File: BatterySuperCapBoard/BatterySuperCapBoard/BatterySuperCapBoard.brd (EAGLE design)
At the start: 94 x 88 mm, 18 parts, among them X1 ESQ-126-38-G-D, X2 WEIDMULLER

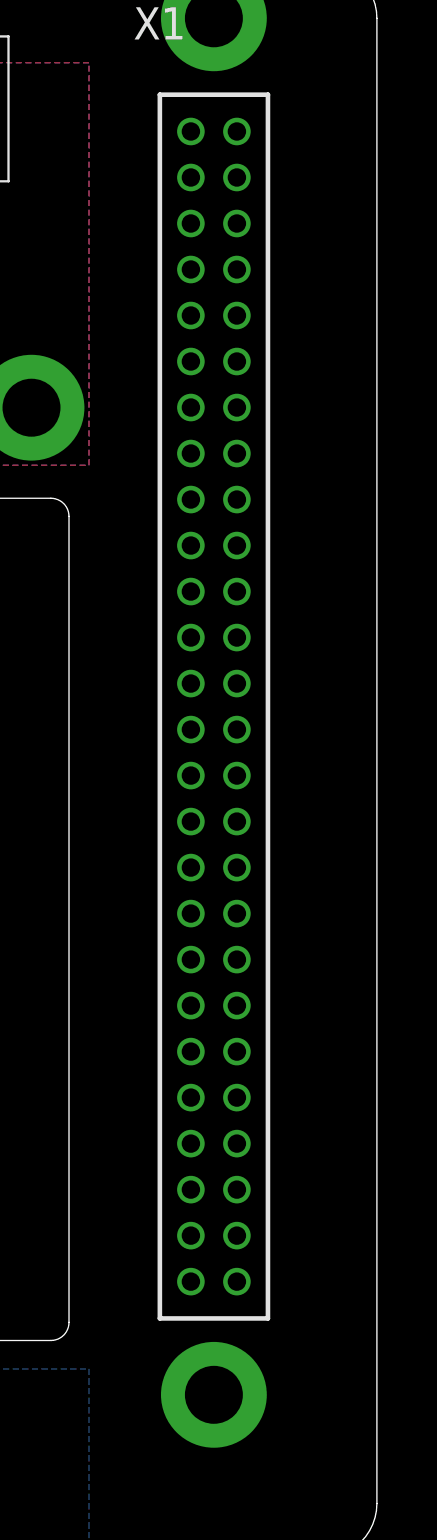
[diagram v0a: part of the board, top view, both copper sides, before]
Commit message: supercap battery board added
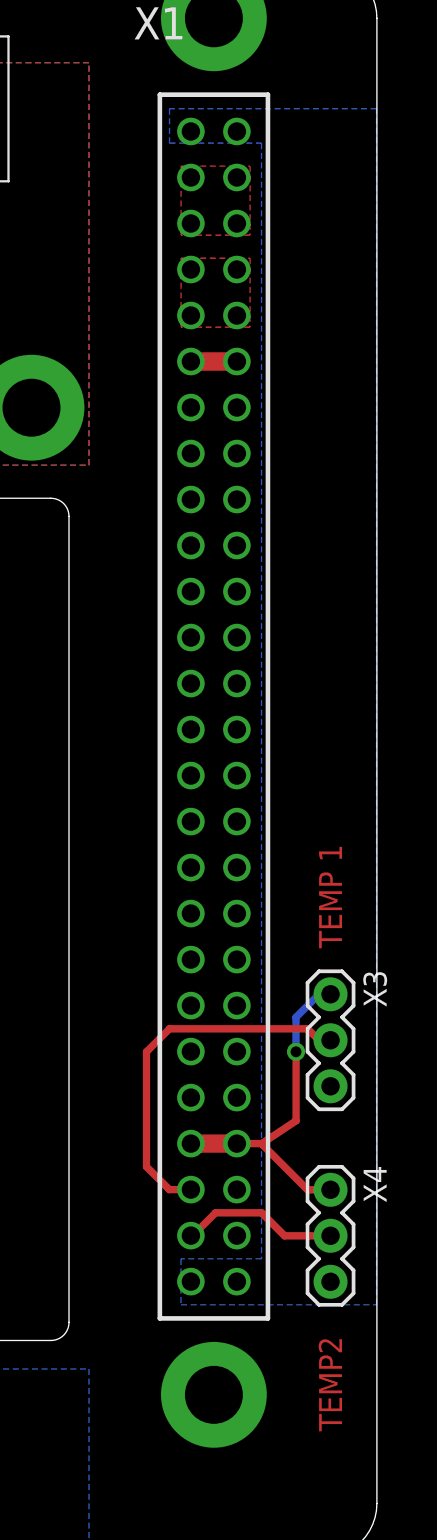
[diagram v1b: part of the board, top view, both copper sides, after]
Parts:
- added X3, X4: (no value), OSSI:1X03
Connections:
- net 3.3VOBC: now also X3.1, X4.1
- net BAT_TEMP: now also X3.2
- net GND: now also X3.3, X4.3
- net SUPERCAP_TEMP: now also X4.2
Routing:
- net BAT_TEMP: track 0.00 -> 20.3 mm
- net 3.3VOBC: track 0.00 -> 19.2 mm, vias 0 -> 1
- net SUPERCAP_TEMP: track 0.00 -> 8.76 mm
- net VBAT: track 0.00 -> 2.54 mm
- added copper zone on layer 16, net GND
- added copper zone on layer 1, net VBUS
- added copper zone on layer 1, net VSOLAR
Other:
- board text added: "TEMP 1"
- board text added: "TEMP2"
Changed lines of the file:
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@@
 <layer number="23" name="tOrigins" color="15" fill="1" visible="yes" active="yes"/>
 <layer number="24" name="bOrigins" color="15" fill="1" visible="yes" active="yes"/>
-<layer number="25" name="tNames" color="7" fill="1" visible="yes" active="yes"/>
-<layer number="26" name="bNames" color="7" fill="1" visible="yes" active="yes"/>
-<layer number="27" name="tValues" color="7" fill="1" visible="yes" active="yes"/>
-<layer number="28" name="bValues" color="7" fill="1" visible="yes" active="yes"/>
-<layer number="29" name="tStop" color="7" fill="3" visible="yes" active="yes"/>
+<layer number="25" name="tNames" color="7" fill="1" visible="no" active="yes"/>
+<layer number="26" name="bNames" color="7" fill="1" visible="no" active="yes"/>
+<layer number="27" name="tValues" color="7" fill="1" visible="no" active="yes"/>
+<layer number="28" name="bValues" color="7" fill="1" visible="no" active="yes"/>
+<layer number="29" name="tStop" color="7" fill="3" visible="no" active="yes"/>
 <layer number="30" name="bStop" color="7" fill="6" visible="no" active="yes"/>
 <layer number="31" name="tCream" color="7" fill="4" visible="no" active="yes"/>
@@
 <wire x1="13" y1="77.5" x2="13" y2="63.5" width="0" layer="20"/>
 <wire x1="13" y1="63.5" x2="14" y2="62.5" width="0" layer="20" curve="90"/>
+<text x="92.075" y="6.985" size="1.27" layer="1" font="vector" rot="R90">TEMP2</text>
+<text x="92.075" y="33.655" size="1.27" layer="1" font="vector" rot="R90">TEMP 1</text>
+<text x="92.075" y="33.655" size="1.27" layer="29" font="vector" rot="R90">TEMP 1</text>
+<text x="92.075" y="6.985" size="1.27" layer="29" font="vector" rot="R90">TEMP2</text>
 </plain>
 <attributes>
@@
 <element name="H15" library="OSSI" package="3.2-PAD-ROUND" value="MOUNT-PAD-ROUND3.2" x="63.5" y="63.5"/>
 <element name="H16" library="OSSI" package="3.2-PAD-ROUND" value="MOUNT-PAD-ROUND3.2" x="74.93" y="63.5"/>
+<element name="X3" library="OSSI" package="1X03" value="" x="91.44" y="31.115" rot="R270"/>
+<element name="X4" library="OSSI" package="1X03" value="" x="91.44" y="20.32" rot="R270"/>
 </elements>
 <signals>
@@
 <contactref element="X1" pad="5"/>
 <contactref element="X1" pad="3"/>
-<wire x1="86.27" y1="73.67" x2="86.27" y2="76.21" width="0" layer="19" extent="1-1"/>
-<wire x1="83.73" y1="76.21" x2="86.27" y2="76.21" width="0" layer="19" extent="1-1"/>
-<wire x1="83.73" y1="73.67" x2="86.27" y2="73.67" width="0" layer="19" extent="1-1"/>
+<polygon width="0.254" layer="1" thermals="no">
+<vertex x="83.185" y="76.835"/>
+<vertex x="86.995" y="76.835"/>
+<vertex x="86.995" y="73.025"/>
+<vertex x="83.185" y="73.025"/>
+</polygon>
 </signal>
 <signal name="GND">
@@
 <contactref element="X1" pad="52"/>
 <contactref element="X1" pad="51"/>
-<wire x1="83.73" y1="78.75" x2="86.27" y2="78.75" width="0" layer="19" extent="1-1"/>
-<wire x1="86.27" y1="15.25" x2="86.27" y2="78.75" width="0" layer="19" extent="1-1"/>
-<wire x1="83.73" y1="15.25" x2="86.27" y2="15.25" width="0" layer="19" extent="1-1"/>
+<contactref element="X4" pad="3"/>
+<contactref element="X3" pad="3"/>
+<polygon width="0.4064" layer="16" isolate="0.6096" thermals="no">
+<vertex x="83.185" y="16.51"/>
+<vertex x="83.185" y="13.97"/>
+<vertex x="93.98" y="13.97"/>
+<vertex x="93.98" y="80.01"/>
+<vertex x="82.55" y="80.01"/>
+<vertex x="82.55" y="78.105"/>
+<vertex x="87.63" y="78.105"/>
+<vertex x="87.63" y="16.51"/>
+</polygon>
 </signal>
 <signal name="3.3VOBC">
 <contactref element="X1" pad="45"/>
 <contactref element="X1" pad="46"/>
-<wire x1="83.73" y1="22.87" x2="86.27" y2="22.87" width="0" layer="19" extent="1-1"/>
+<wire x1="83.73" y1="22.87" x2="86.27" y2="22.87" width="1.016" layer="1"/>
+<contactref element="X4" pad="1"/>
+<contactref element="X3" pad="1"/>
+<wire x1="86.27" y1="22.87" x2="87.62" y2="22.87" width="0.4064" layer="1"/>
+<wire x1="87.62" y1="22.87" x2="90.17" y2="20.32" width="0.4064" layer="1"/>
+<wire x1="90.17" y1="20.32" x2="91.44" y2="20.32" width="0.4064" layer="1"/>
+<wire x1="87.62" y1="22.87" x2="87.64" y2="22.87" width="0.4064" layer="1"/>
+<wire x1="87.64" y1="22.87" x2="89.535" y2="24.13" width="0.4064" layer="1"/>
+<wire x1="89.535" y1="24.13" x2="89.535" y2="27.94" width="0.4064" layer="1"/>
+<via x="89.535" y="27.94" extent="1-16" drill="0.6"/>
+<wire x1="89.535" y1="27.94" x2="89.535" y2="29.845" width="0.4064" layer="16"/>
+<wire x1="89.535" y1="29.845" x2="90.805" y2="31.115" width="0.4064" layer="16"/>
+<wire x1="91.44" y1="31.115" x2="90.805" y2="31.115" width="0.4064" layer="16"/>
 </signal>
 <signal name="PANELTEMP_SCL">
@@
 <contactref element="X1" pad="7"/>
 <contactref element="X1" pad="9"/>
-<wire x1="86.27" y1="68.59" x2="86.27" y2="71.13" width="0" layer="19" extent="1-1"/>
-<wire x1="83.73" y1="71.13" x2="86.27" y2="71.13" width="0" layer="19" extent="1-1"/>
-<wire x1="83.73" y1="68.59" x2="86.27" y2="68.59" width="0" layer="19" extent="1-1"/>
+<polygon width="0.254" layer="1" thermals="no">
+<vertex x="83.185" y="71.755"/>
+<vertex x="86.995" y="71.755"/>
+<vertex x="86.995" y="67.945"/>
+<vertex x="83.185" y="67.945"/>
+</polygon>
 </signal>
 <signal name="VBAT">
 <contactref element="X1" pad="11"/>
 <contactref element="X1" pad="12"/>
-<wire x1="83.73" y1="66.05" x2="86.27" y2="66.05" width="0" layer="19" extent="1-1"/>
+<wire x1="83.73" y1="66.05" x2="86.27" y2="66.05" width="1.016" layer="1"/>
 </signal>
 <signal name="VSUPERCAP">
@@
 <signal name="BAT_TEMP">
 <contactref element="X1" pad="47"/>
+<contactref element="X3" pad="2"/>
+<wire x1="83.73" y1="20.33" x2="82.54" y2="20.33" width="0.4064" layer="1"/>
+<wire x1="82.54" y1="20.33" x2="81.28" y2="21.59" width="0.4064" layer="1"/>
+<wire x1="81.28" y1="21.59" x2="81.28" y2="27.94" width="0.4064" layer="1"/>
+<wire x1="81.28" y1="27.94" x2="82.55" y2="29.21" width="0.4064" layer="1"/>
+<wire x1="82.55" y1="29.21" x2="90.17" y2="29.21" width="0.4064" layer="1"/>
+<wire x1="91.44" y1="28.575" x2="90.805" y2="28.575" width="0.4064" layer="1"/>
+<wire x1="90.805" y1="28.575" x2="90.17" y2="29.21" width="0.4064" layer="1"/>
 </signal>
 <signal name="SUPERCAP_TEMP">
 <contactref element="X1" pad="49"/>
+<contactref element="X4" pad="2"/>
+<wire x1="83.73" y1="17.79" x2="83.83" y2="17.79" width="0.4064" layer="1"/>
+<wire x1="83.83" y1="17.79" x2="85.09" y2="19.05" width="0.4064" layer="1"/>
+<wire x1="85.09" y1="19.05" x2="87.63" y2="19.05" width="0.4064" layer="1"/>
+<wire x1="87.63" y1="19.05" x2="88.9" y2="17.78" width="0.4064" layer="1"/>
+<wire x1="88.9" y1="17.78" x2="91.44" y2="17.78" width="0.4064" layer="1"/>
 </signal>
 <signal name="N$1">
